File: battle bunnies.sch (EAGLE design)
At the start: 45 parts, among them IC1 CP2104, Q1 mmbt2222, Q2 mmbt2222, SW2 KMR2, U1 BME280, U2 SPX3819, U3 MCP73831T-2ACI/OT, X2 ESP-12, X4 20329

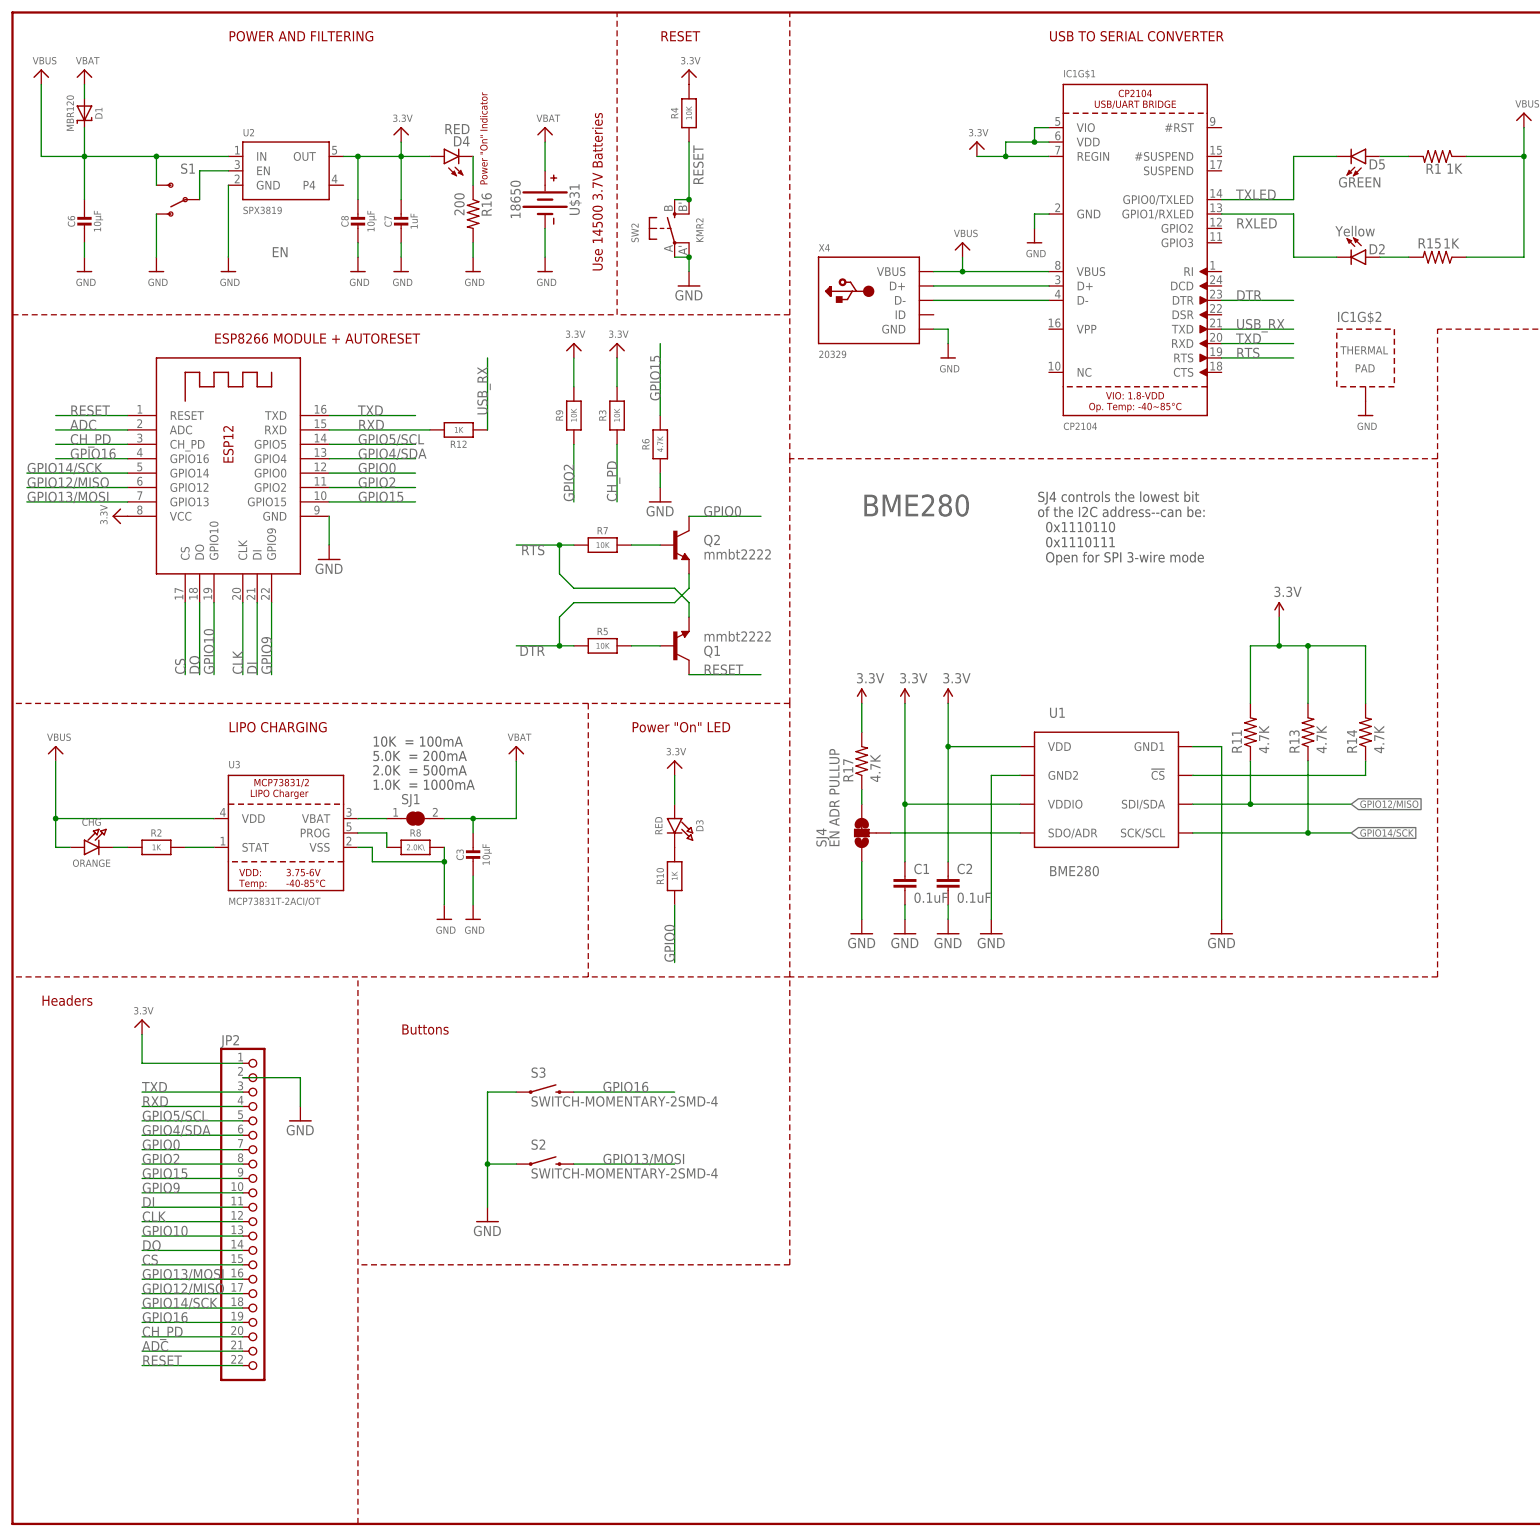
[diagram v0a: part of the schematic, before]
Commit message: Initial commit for ESP32 conversion
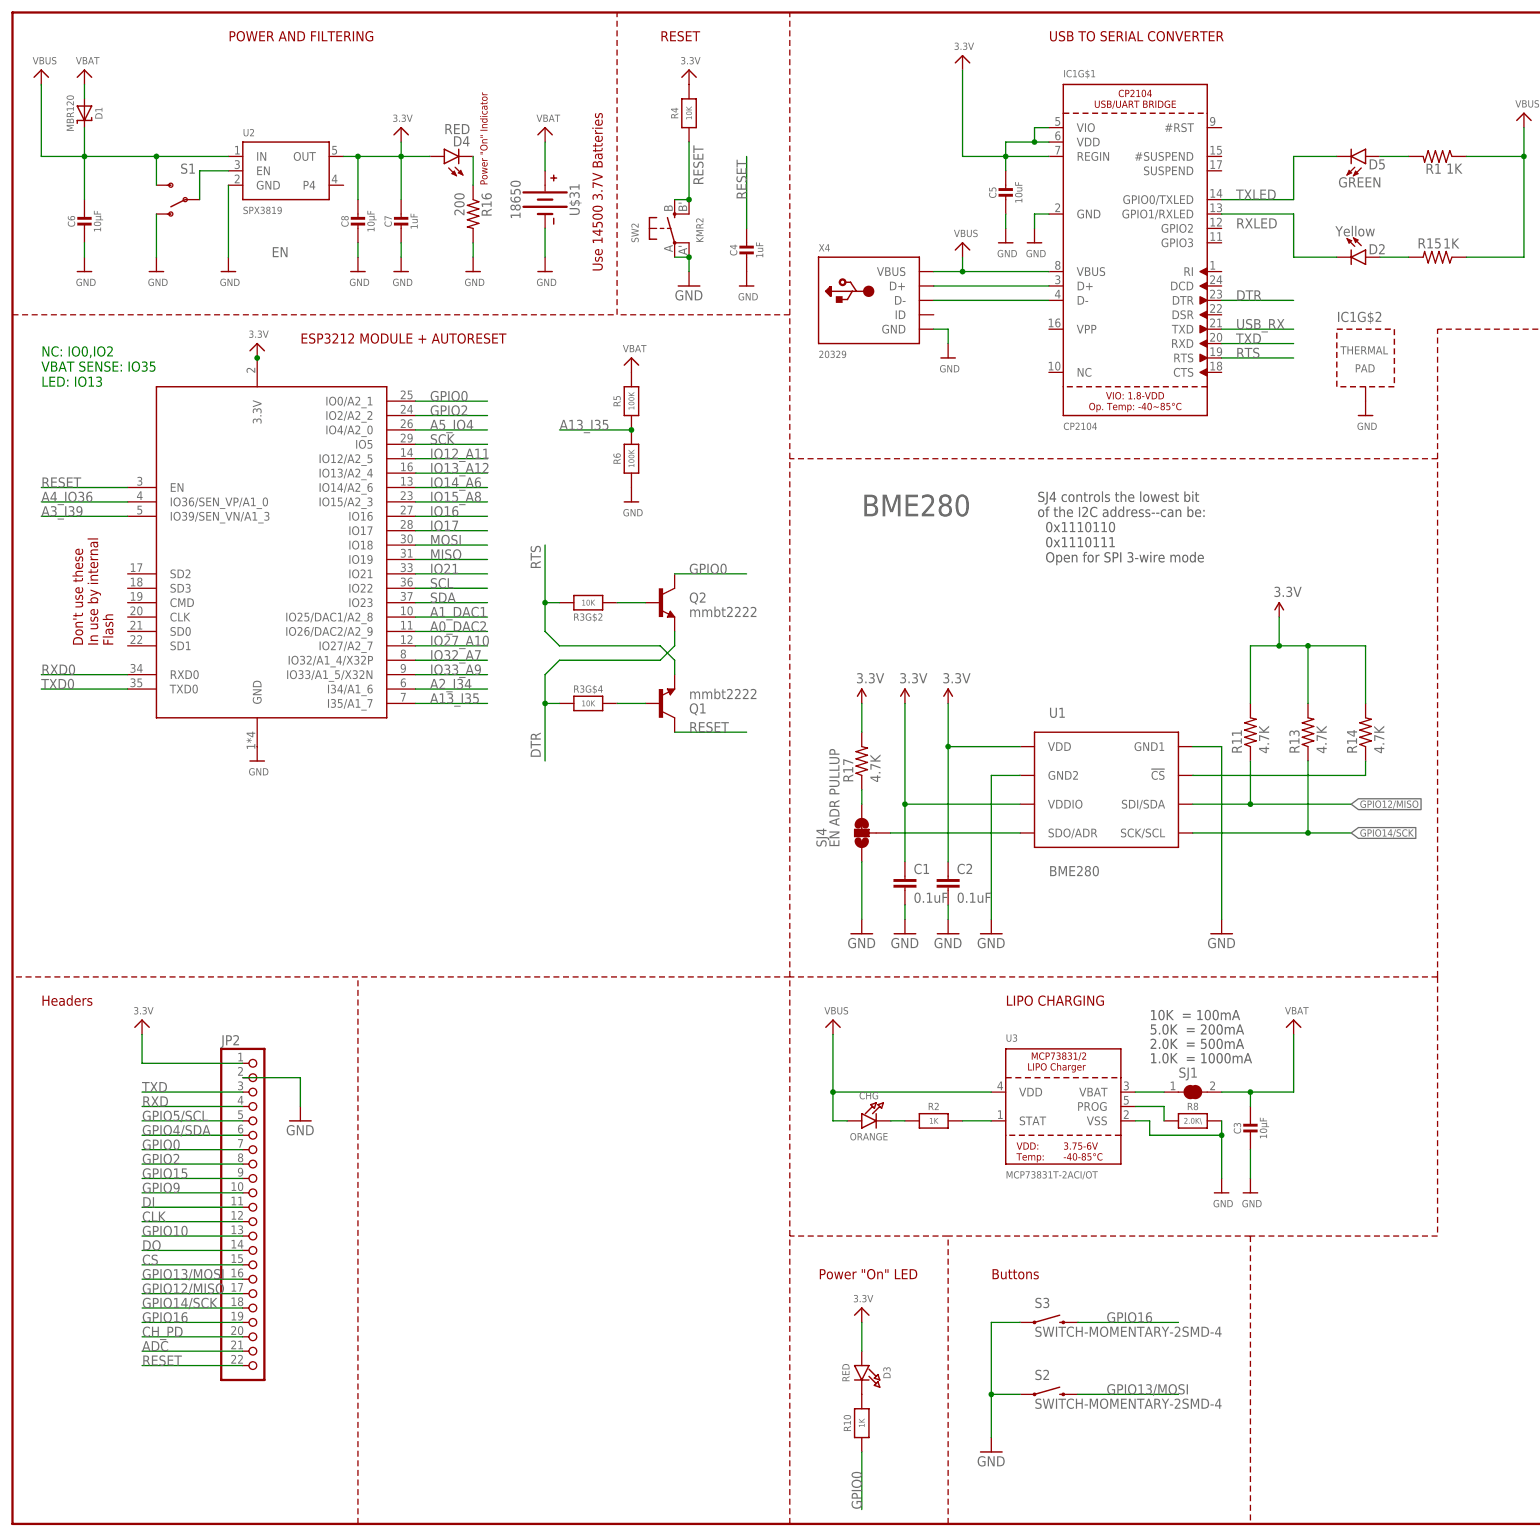
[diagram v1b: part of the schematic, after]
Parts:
- removed R12: 1K, microbuilder:RESISTOR_0603MP
- removed R7: 10K, microbuilder:RESISTOR_0603MP
- removed R9: 10K, microbuilder:RESISTOR_0603_NOOUT
- added C4: 1uF, microbuilder:CAP_CERAMIC0603_NO
- added C5: 10uF, microbuilder:CAP_CERAMIC0805-NOOUTLINE
- R3: device microbuilder:RESISTOR_0603_NOOUT -> microbuilder:RESISTOR_4PACK
- R5: value 10K -> 100K
- R6: value 4.7K -> 100K
- X2: value ESP-12 -> ESP32_WROOM32_SKINNY; device microbuilder:ESP-12E -> microbuilder:ESP32_WROOM32_SKINNY
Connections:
- new net A0_DAC2: X2.IO26/DAC2/A2_9
- new net A13_I35: R5.1, R6.2, X2.I35/A1_7
- new net A1_DAC1: X2.IO25/DAC1/A2_8
- new net A2_I34: X2.I34/A1_6
- new net A3_I39: X2.IO39/SEN_VN/A1_3
- new net A4_IO36: X2.IO36/SEN_VP/A1_0
- new net A5_IO4: X2.IO4/A2_0
- new net IO12_A11: X2.IO12/A2_5
- new net IO13_A12: X2.IO13/A2_4
- new net IO14_A6: X2.IO14/A2_6
- new net IO15_A8: X2.IO15/A2_3
- new net IO16: X2.IO16
- new net IO17: X2.IO17
- new net IO21: X2.IO21
- new net IO27_A10: X2.IO27/A2_7
- new net IO32_A7: X2.IO32/A1_4/X32P
- new net IO33_A9: X2.IO33/A1_5/X32N
- new net MISO: X2.IO19
- new net MOSI: X2.IO18
- new net RXD0: X2.RXD0
- new net SCK: X2.IO5
- new net SCL: X2.IO22
- new net SDA: X2.IO23
- new net TXD0: X2.TXD0
- net 3.3V: now also C5.1, X2.3.3V; no longer R3.2, R9.2, X2.VCC
- net ADC: no longer X2.ADC
- net CH_PD: no longer R3.1, X2.CH_PD
- net CLK: no longer X2.CLK
- net CS: no longer X2.CS
- net DI: no longer X2.DI
- net DO: no longer X2.DO
- net DTR: now also R3G$4.1; no longer R5.1
- net GND: now also C4.2, C5.2
- net GPIO0: now also X2.IO0/A2_1; no longer X2.GPIO0
- net GPIO10: no longer X2.GPIO10
- net GPIO12/MISO: no longer X2.GPIO12
- net GPIO13/MOSI: no longer X2.GPIO13
- net GPIO14/SCK: no longer X2.GPIO14
- net GPIO15: no longer R6.2, X2.GPIO15
- net GPIO16: no longer X2.GPIO16
- net GPIO2: now also X2.IO2/A2_2; no longer R9.1, X2.GPIO2
- net GPIO4/SDA: no longer X2.GPIO4
- net GPIO5/SCL: no longer X2.GPIO5
- net GPIO9: no longer X2.GPIO9
- net N$12: now also R3G$4.2; no longer R5.2
- net N$13: now also R3G$2.1; no longer R7.2
- net RESET: now also C4.1, X2.EN; no longer X2.RESET
- net RTS: now also R3G$2.2; no longer R7.1
- net RXD: no longer R12.2, X2.RXD
- net TXD: no longer X2.TXD
- net USB_RX: no longer R12.1
- net VBAT: now also R5.2
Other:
- note added: "Don't use these In use by internal Flash"
- note added: "ESP3212 MODULE + AUTORESET"
- note added: "NC: IO0,IO2 VBAT SENSE: IO35 LED: IO13"
- note removed: "ESP8266 MODULE + AUTORESET"
- moved on the sheet: C3, CHG, D3, Q1, Q2, R10, R2, R5, R6, R8, S2, S3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

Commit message: Initial, full, routing - minus Sensors, update gitignore
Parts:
- removed C1, C2: 0.1uF, SparkFun-Capacitors:0.1UF-25V-5%(0603)
- removed D1: MBR120, microbuilder:DIODE-SCHOTTKYSOD-123
- removed R11, R13, R14, R17: 4.7K, SparkFun-Resistors:4.7KOHM-1/10W-1%(0603)
- removed R16: 200, SparkFun-Resistors:200OHM1/10W1%(0603)
- removed SJ4: EN ADR PULLUP, SparkFun-Passives:JUMPER-PAD-3-2OF3_NC_BY_TRACE_SMALL
- removed U1: BME280, BME280ComponentLibrary:BME280
- added C9: 10uF, microbuilder:CAP_CERAMIC0805-NOOUTLINE
- added JP3: JUMPER-SMT_2_NC_TRACE_SILK, SparkFun-Jumpers:JUMPER-SMT_2_NC_TRACE_SILK
- added Q3: DMG3415U, microbuilder:MOSFET-P
- added R12, R7: 100K, microbuilder:RESISTOR_0603_NOOUT
- added R9: 10k, SparkFun-Resistors:10KOHM-0603-1/10W-1%
- D4: value RED -> MBR120; device SparkFun-LED:LED-RED0603 -> microbuilder:DIODE-SCHOTTKYSOD-123
- JP2: device pinhead:PINHD-1X22 -> SparkFun-Connectors:CONN_29
- R3: value 10K -> 10k; device microbuilder:RESISTOR_4PACK -> SparkFun-Resistors:10KOHM-0603-1/10W-1%
- U2: value SPX3819 -> AP2112-3.3
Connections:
- removed net !CS: R14.1, U1.!CS
- removed net ADC: JP2.21
- removed net CH_PD: JP2.20
- removed net CLK: JP2.12
- removed net CS: JP2.15
- removed net DI: JP2.11
- removed net DO: JP2.14
- removed net GPIO10: JP2.13
- removed net GPIO12/MISO: JP2.17, R11.1, U1.SDI/SDA
- removed net GPIO13/MOSI: JP2.16, S2.2
- removed net GPIO14/SCK: JP2.18, R13.1, U1.SCK/SCL
- removed net GPIO15: JP2.9
- removed net GPIO16: JP2.19, S3.2
- removed net GPIO4/SDA: JP2.6
- removed net GPIO5/SCL: JP2.5
- removed net GPIO9: JP2.10
- removed net IO21: X2.IO21
- removed net N$11: D4.A
- removed net N$15: R17.1, SJ4.3
- removed net RXD: JP2.4
- removed net SDO/ADR: SJ4.2, U1.SDO/ADR
- removed net TXD: IC1G$1.RXD, JP2.3
- removed net USB_RX: IC1G$1.TXD
- new net IO23: JP2.17, X2.IO23
- new net N$6: C5.1, IC1G$1.REGIN, IC1G$1.VDD, IC1G$1.VIO, JP3.1
- new net N$7: C6.1, D4.C, Q3.S, R7.2, U2.IN
- net 3.3V: now also C9.1, JP3.2; no longer C1.1, C2.1, C5.1, IC1G$1.REGIN, IC1G$1.VDD, IC1G$1.VIO, R11.2, R13.2, R14.2, R17.2, U1.VDD, U1.VDDIO
- net A0_DAC2: now also JP2.25
- net A1_DAC1: now also JP2.24
- net A2_I34: now also JP2.21
- net A3_I39: now also JP2.19
- net A4_IO36: now also JP2.18
- net A5_IO4: now also JP2.8, S2.2
- net DTR: now also R9.1; no longer R3G$4.1
- net EN: now also JP2.7
- net GND: now also C9.2, JP2.4, JP2.6, R12.1; no longer C1.2, C2.2, R16.2, SJ4.1, U1.GND1, U1.GND2
- net GPIO0: no longer JP2.7
- net GPIO2: now also S3.2; no longer JP2.8
- net IO12_A11: now also JP2.28
- net IO13_A12: now also JP2.20
- net IO14_A6: now also JP2.27
- net IO15_A8: now also JP2.10
- net IO16: now also JP2.9
- net IO17: now also JP2.11
- net IO27_A10: now also JP2.26
- net IO32_A7: now also JP2.22
- net IO33_A9: now also JP2.23
- net MISO: now also JP2.14
- net MOSI: now also JP2.13
- net N$12: now also R9.2; no longer R3G$4.2
- net N$13: now also R3.2; no longer R3G$2.1
- net N$4: now also R7.1, S1.S; no longer D4.C, R16.1
- net RESET: now also JP2.29; no longer JP2.22
- net RTS: now also R3.1; no longer R3G$2.2
- net RXD0: now also IC1G$1.TXD
- net SCK: now also JP2.12
- net SCL: now also JP2.16
- net SDA: now also JP2.15, X2.IO21; no longer X2.IO23
- net TXD0: now also IC1G$1.RXD
- net VBAT: now also JP2.5, Q3.D; no longer D1.A
- net VBUS: now also D4.A, JP2.3, Q3.G, R12.2; no longer C6.1, D1.C, S1.S, U2.IN
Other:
- note added: "GPIO Table (What's Used, What's Available) ------------------------ GPIO00/Touch1/ADC2_1/CLK01 GPIO01/HS2D1/U0TXD/CLK03 GPIO02/Touch2/ADC2_2/HSPIWP - Button GPIO03/HS2D0/U0RXD/CLK02 GPIO04/Touch0/ADC2_0/HSPIHD - Button GPIO05/HS1D6/VSPICS0/(WIRE SPI SS) GPIO06/U1CTS/SDCLK/HS1CLK/SPICLK GPIO07/SDD0/HS1D0/SPIQ GPIO08/SDD1/HS1D1/SPI GPIO09/SPIHD/HS1D2/SDD2/U1RXD GPIO10/SPIWP/HS1D3/SDD3/U1TXD GPIO11/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"
- note added: "Header"
- note added: "Use 18650 3.7V Batteries"
- note removed: "BME280"
- note removed: "GPIO Table (What's Used, What's Available) ------------------------ GPIO0 - LED (schematic) GPIO02/ - GPIO4/SDA/PWM - GPIO5/SCL/IR Rx - IR Rx GPIO9 - PCA9865 GPIO10 - PCA9865 GPIO12/MISO/PWM/IR Tx - IR Tx GPIO13/MOSI - GPIO14/SCL/PWM - GPIO15/CS/PWM - Button GPIO16 - Button ADC - Total: 17 GPIOs, 2 taken for UART (15). I count 14 pinned now"
- note removed: "Headers"
- note removed: "Power "On" Indicator"
- note removed: "SJ4 controls the lowest bit of the I2C address--can be: 0x1110110 0x1110111 Open for SPI 3-wire mode"
- note removed: "Use 14500 3.7V Batteries"
- moved on the sheet: C6, C7, C8, S1, U$31, U2
